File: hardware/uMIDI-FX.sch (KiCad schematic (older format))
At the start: 0 parts

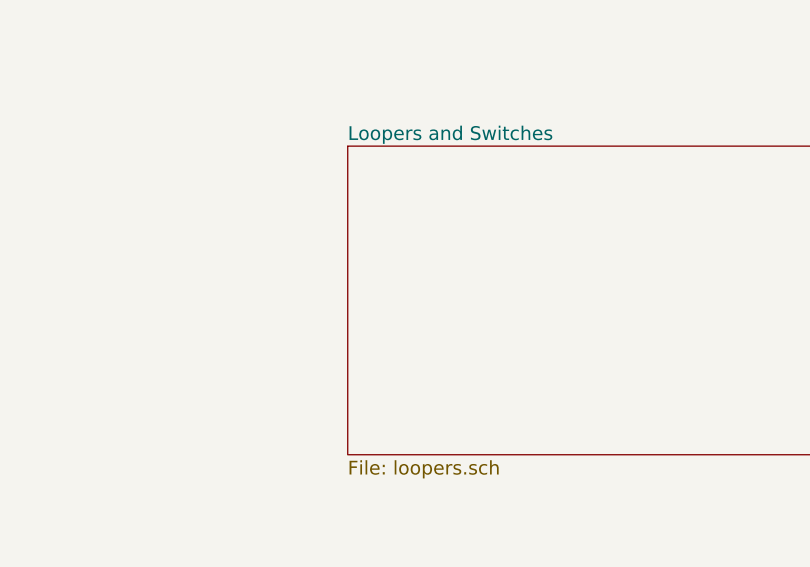
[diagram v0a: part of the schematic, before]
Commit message: Draw looper chain
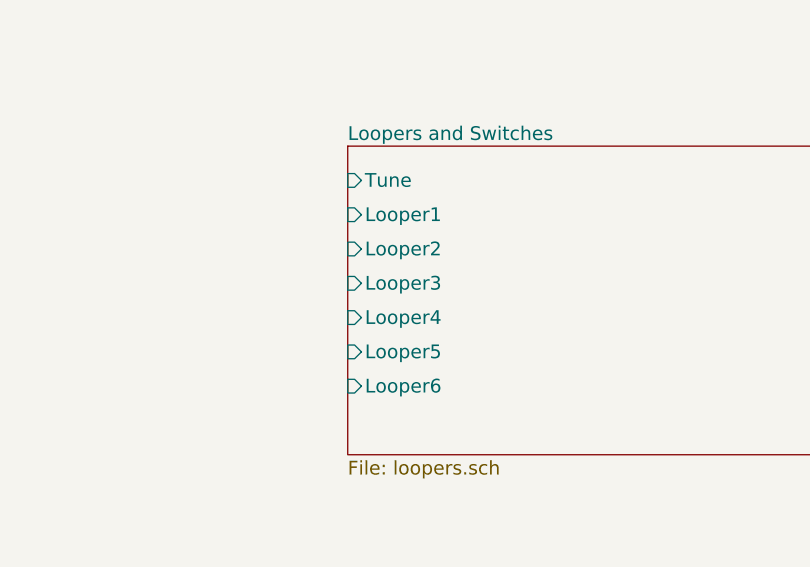
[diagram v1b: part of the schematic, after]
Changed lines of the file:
@@
 F0 "Loopers and Switches" 60
 F1 "loopers.sch" 60
+F2 "Tune" I L 5150 2050 60
+F3 "Looper1" I L 5150 2200 60
+F4 "Looper2" I L 5150 2350 60
+F5 "Looper3" I L 5150 2500 60
+F6 "Looper4" I L 5150 2650 60
+F7 "Looper5" I L 5150 2800 60
+F8 "Looper6" I L 5150 2950 60
 $EndSheet
 $Sheet
@@
 F1 "wah.sch" 60
 F2 "9V_Wah" I L 1900 4500 60
-F4 "PWM" I L 1900 4650 60
-F5 "Bypass" I L 1900 4800 60
+F3 "PWM" I L 1900 4650 60
+F4 "Bypass" I L 1900 4800 60
 $EndSheet
 $EndSCHEMATC

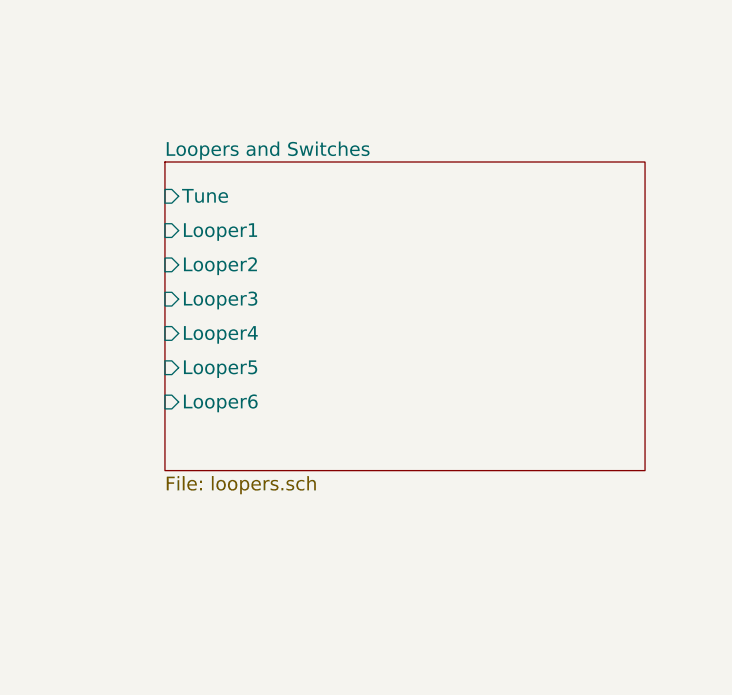
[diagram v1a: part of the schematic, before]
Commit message: Stub and integrate aux switch
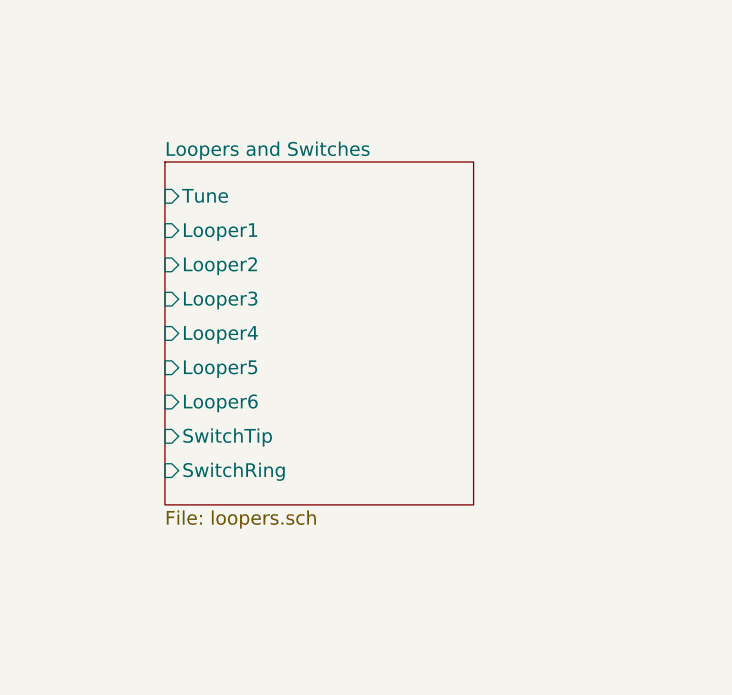
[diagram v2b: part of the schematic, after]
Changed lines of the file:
@@
 $Descr A4 11693 8268
 encoding utf-8
-Sheet 1 19
+Sheet 1 21
 Title ""
 Date ""
@@
 F0 "HMI" 60
 F1 "hmi.sch" 60
-$EndSheet
-$Sheet
-S 5150 1900 2100 1350
-U 54D120FF
-F0 "Loopers and Switches" 60
-F1 "loopers.sch" 60
-F2 "Tune" I L 5150 2050 60
-F3 "Looper1" I L 5150 2200 60
-F4 "Looper2" I L 5150 2350 60
-F5 "Looper3" I L 5150 2500 60
-F6 "Looper4" I L 5150 2650 60
-F7 "Looper5" I L 5150 2800 60
-F8 "Looper6" I L 5150 2950 60
 $EndSheet
 $Sheet
@@
 F4 "Bypass" I L 1900 4800 60
 $EndSheet
+$Sheet
+S 5150 1900 1350 1500
+U 54D120FF
+F0 "Loopers and Switches" 60
+F1 "loopers.sch" 60
+F2 "Tune" I L 5150 2050 60
+F3 "Looper1" I L 5150 2200 60
+F4 "Looper2" I L 5150 2350 60
+F5 "Looper3" I L 5150 2500 60
+F6 "Looper4" I L 5150 2650 60
+F7 "Looper5" I L 5150 2800 60
+F8 "Looper6" I L 5150 2950 60
+F9 "SwitchTip" I L 5150 3100 60
+F10 "SwitchRing" I L 5150 3250 60
+$EndSheet
 $EndSCHEMATC
